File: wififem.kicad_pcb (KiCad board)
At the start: 2 copper layers, 40 x 49.5 mm, 44 parts, among them J1 Conn_Coaxial, J2 Conn_Coaxial, J3 Conn_Coaxial, J4 Conn_01x05, U1 MCP6566, U2 74HCT04, U3 SE2611T, U4 AP1117-15

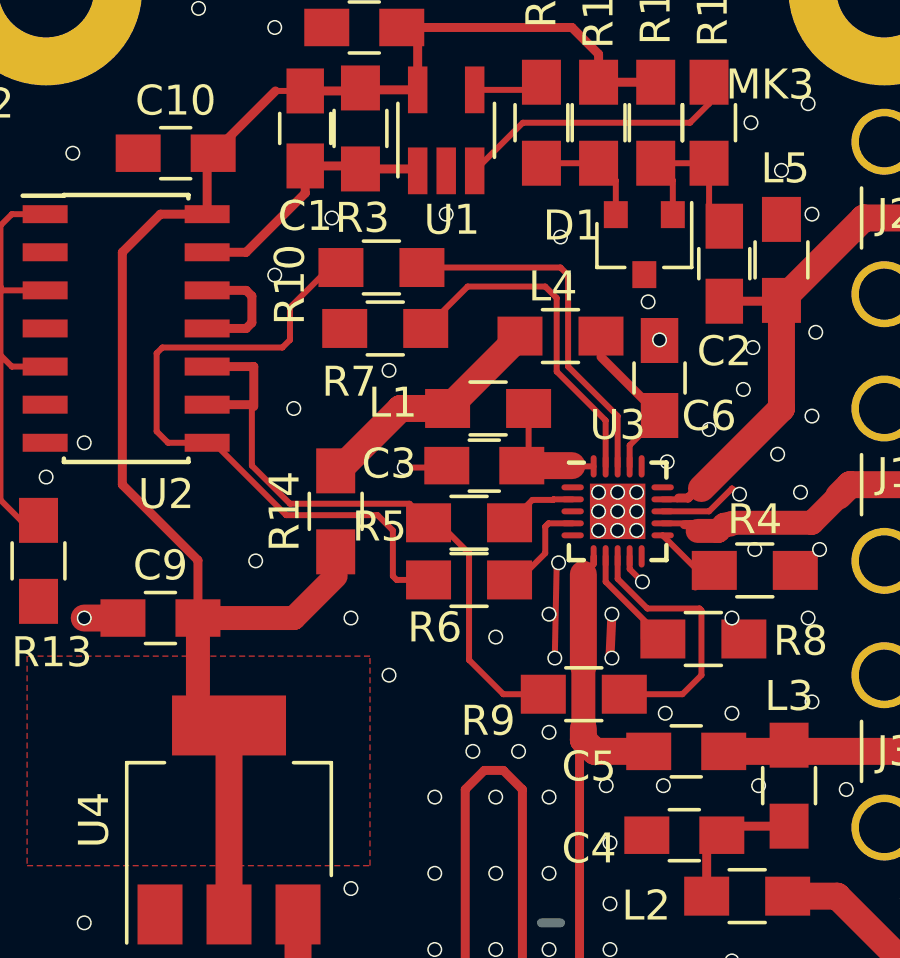
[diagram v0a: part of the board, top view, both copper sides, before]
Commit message: Add LNA on/off jumper
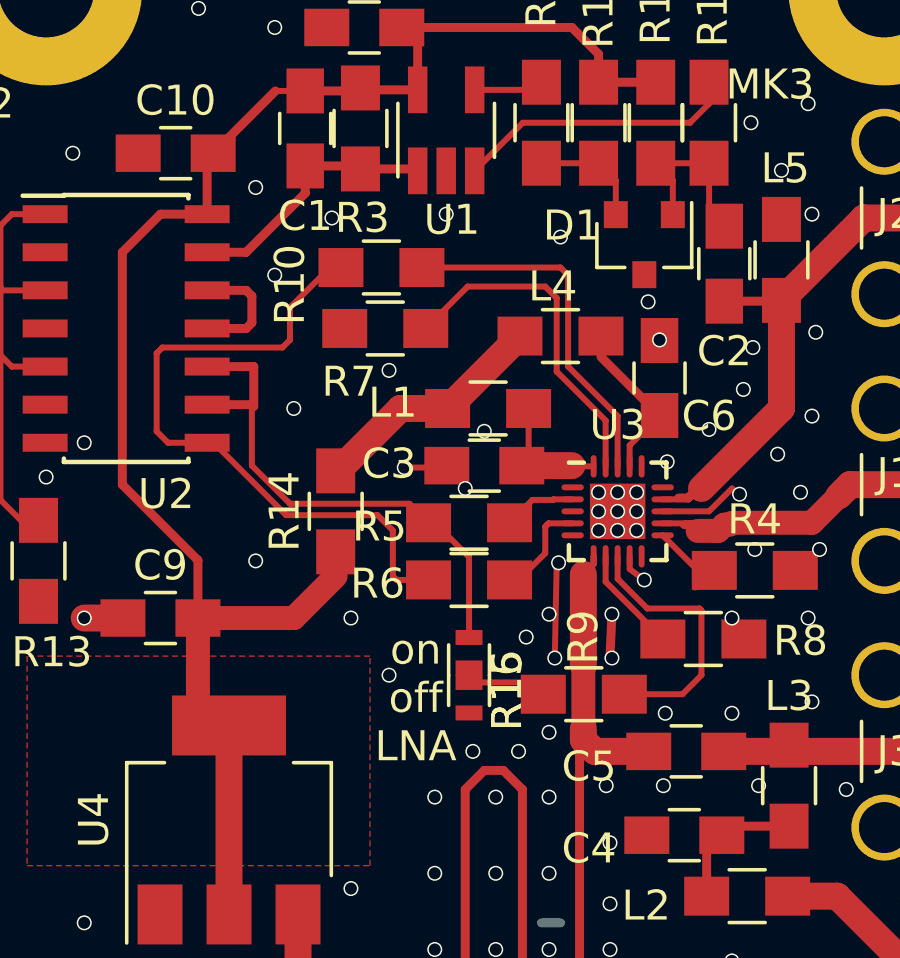
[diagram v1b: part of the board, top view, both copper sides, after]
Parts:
- added R15: 0 (lna off), Resistors_SMD:R_0603, F.Cu at (104.9, 71.4)
- added R16: 0 (lna on), Resistors_SMD:R_0603, F.Cu at (104.9, 70.4)
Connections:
- R5 pad 1: Net-(R5-Pad1) -> Net-(R16-Pad1)
- R9 pad 1: Net-(R5-Pad1) -> Net-(R15-Pad1)
- U2 pad 10: Net-(R5-Pad1) -> Net-(R16-Pad1)
- U2 pad 9: Net-(R5-Pad1) -> Net-(R16-Pad1)
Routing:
- net Net-(R5-Pad1): track 21.5 -> 0.00 mm
- net Net-(R16-Pad1): track 0.00 -> 18.5 mm
- net Net-(R15-Pad1): track 0.00 -> 2.74 mm
- net GND: vias 127 -> 130
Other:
- board text added: "on off LNA"

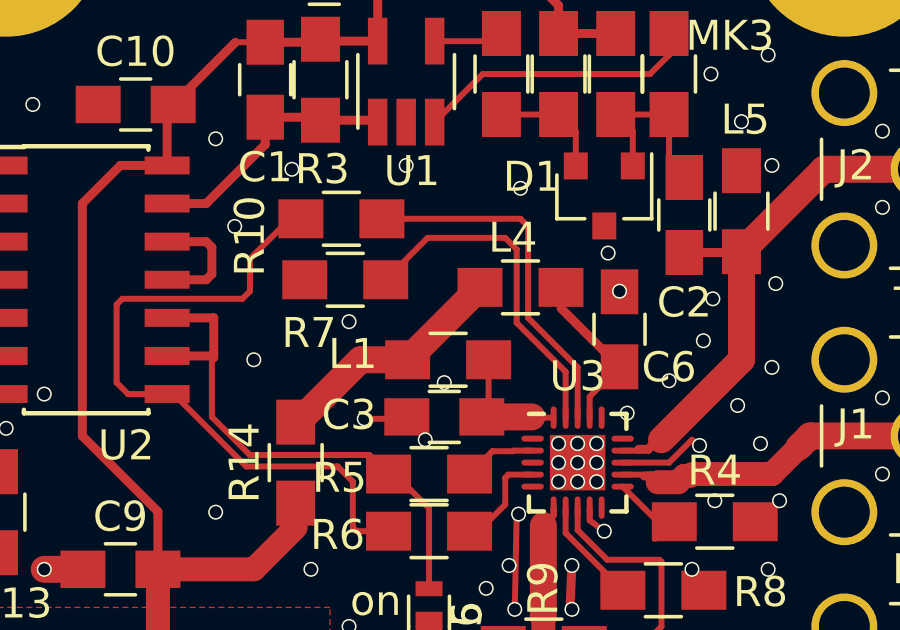
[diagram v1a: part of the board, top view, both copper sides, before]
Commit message: Power supply decoupling as suggested
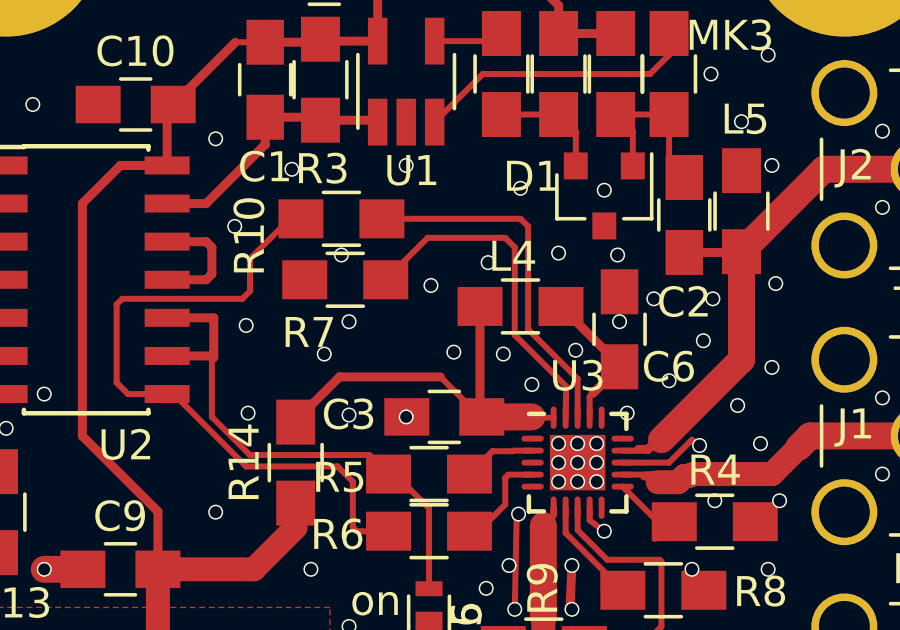
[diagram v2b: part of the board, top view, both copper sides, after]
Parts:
- removed L1: ferrite bead, Inductors_SMD:L_0805_HandSoldering
- moved L4 0.63 mm to (108.0, 60.2)
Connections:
- L4 pad 1: Net-(L1-Pad1) -> Net-(C3-Pad2)
- R14 pad 2: Net-(L1-Pad1) -> Net-(C3-Pad2)
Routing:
- net Net-(C3-Pad2): track 4.40 -> 13.9 mm
- net Net-(L1-Pad1): track 8.00 -> 0.00 mm
- net GND: track 11.4 -> 10.0 mm, vias 130 -> 141
- net Net-(C6-Pad2): track 5.62 -> 4.99 mm

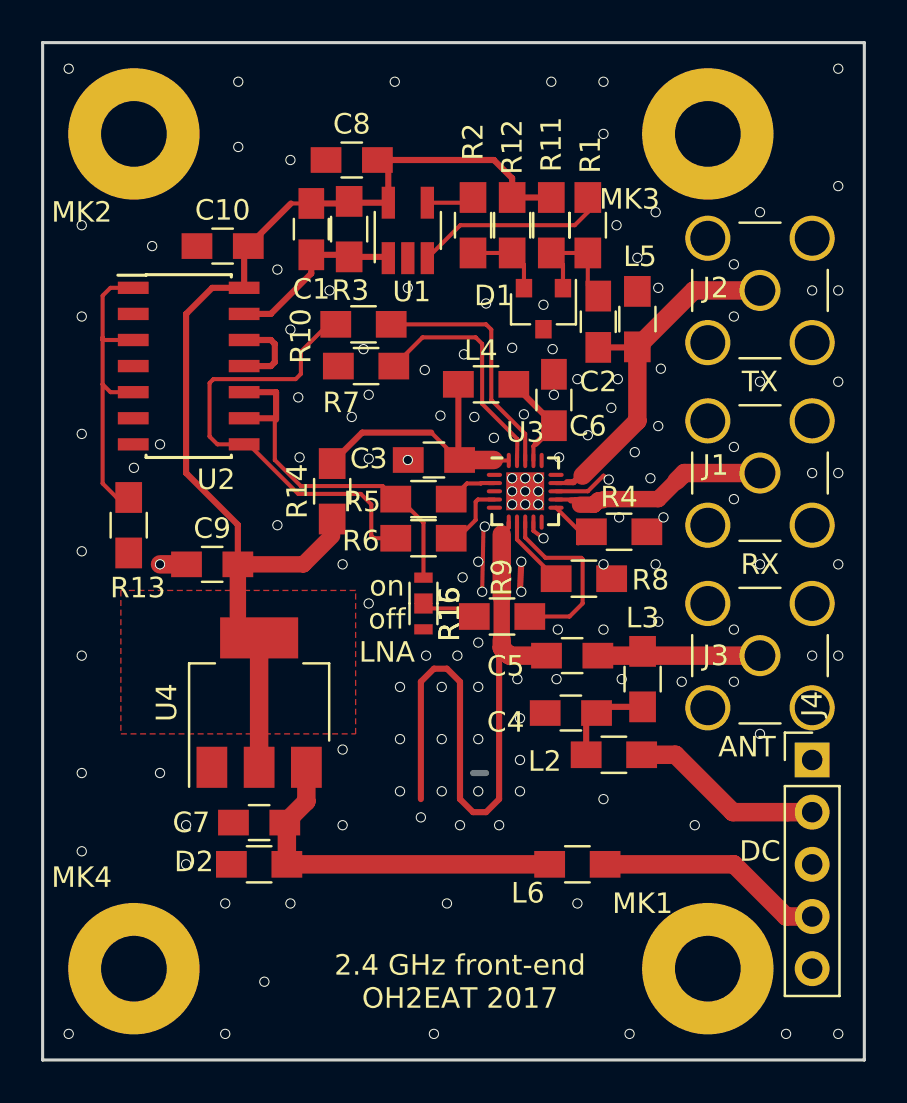
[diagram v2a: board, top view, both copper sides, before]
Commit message: Increased clearance for non-RF traces
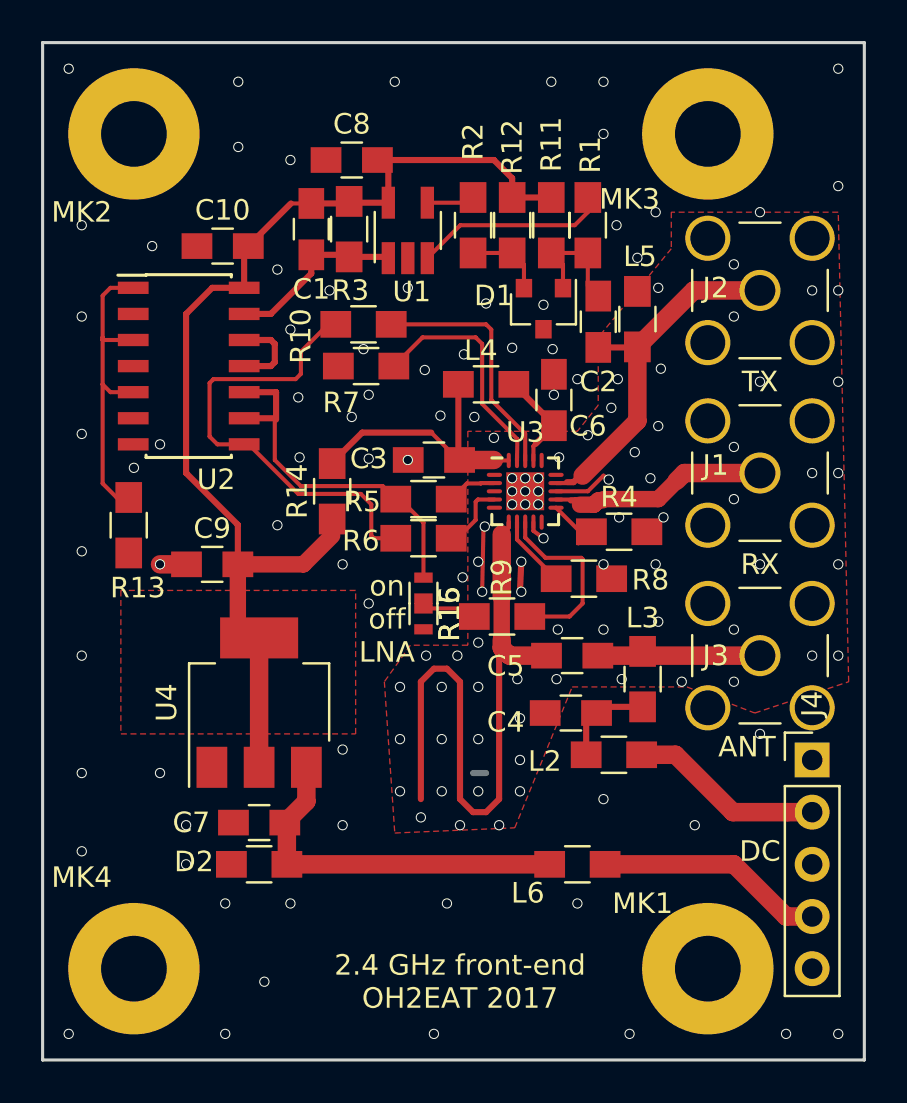
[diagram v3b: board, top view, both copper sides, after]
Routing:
- net GND: vias 141 -> 140
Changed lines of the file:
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@@
     (thickness 1.6)
     (drawings 10)
-    (tracks 372)
+    (tracks 371)
     (zones 0)
     (modules 45)
@@
     (35 F.Paste user hide)
     (36 B.SilkS user hide)
-    (37 F.SilkS user)
+    (37 F.SilkS user hide)
     (38 B.Mask user hide)
     (39 F.Mask user hide)
@@
     (user_trace_width 0.9)
     (trace_clearance 0.1524)
-    (zone_clearance 0)
+    (zone_clearance 0.5)
     (zone_45_only yes)
     (trace_min 0.2)
@@
   (via (at 107.3785 61.7855) (size 0.5) (drill 0.4) (layers F.Cu B.Cu) (net 4))
   (via (at 108.331 62.8015) (size 0.5) (drill 0.4) (layers F.Cu B.Cu) (net 4))
-  (via (at 109.7915 61.6585) (size 0.5) (drill 0.4) (layers F.Cu B.Cu) (net 4))
   (via (at 102.235 63.8175) (size 0.5) (drill 0.4) (layers F.Cu B.Cu) (net 4))
   (via (at 97.79 54.61) (size 0.5) (drill 0.4) (layers F.Cu B.Cu) (net 4))
@@
   (segment (start 107.37724 71.501) (end 107.27724 71.501) (width 0.2) (layer F.Cu) (net 38))
   (zone (net 4) (net_name GND) (layer F.Cu) (hatch edge 0.508)
-    (connect_pads yes (clearance 0.2))
+    (connect_pads yes (clearance 0.5))
     (min_thickness 0.2)
     (fill yes (arc_segments 16) (thermal_gap 0.5) (thermal_bridge_width 0.5))
@@
       )
     )
+  )
+  (zone (net 4) (net_name GND) (layer F.Cu) (hatch edge 0.508)
+    (priority 1)
+    (connect_pads yes (clearance 0.2))
+    (min_thickness 0.2)
+    (fill yes (arc_segments 16) (thermal_gap 0.5) (thermal_bridge_width 0.5))
+    (polygon
+      (pts
+        (xy 125.095 51.816) (xy 116.967 51.816) (xy 116.967 53.594) (xy 113.411 57.912) (xy 113.411 61.214)
+        (xy 112.395 62.484) (xy 107.061 62.484) (xy 107.061 72.898) (xy 104.267 72.898) (xy 102.997 74.676)
+        (xy 103.505 82.042) (xy 109.347 81.788) (xy 112.141 74.93) (xy 117.729 74.93) (xy 121.031 76.2)
+        (xy 125.603 74.676)
+      )
+    )

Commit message: Moved some components a bit
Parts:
- moved L4 0.64 mm to (107.3, 60.2)
- moved C6 0.44 mm to (110.8, 61.0)
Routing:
- net Net-(C6-Pad2): track 4.99 -> 7.08 mm
- net Net-(C5-Pad2): track 33.3 -> 32.7 mm
- net Net-(R10-Pad2): track 12.0 -> 11.5 mm
- net GND: vias 140 -> 141

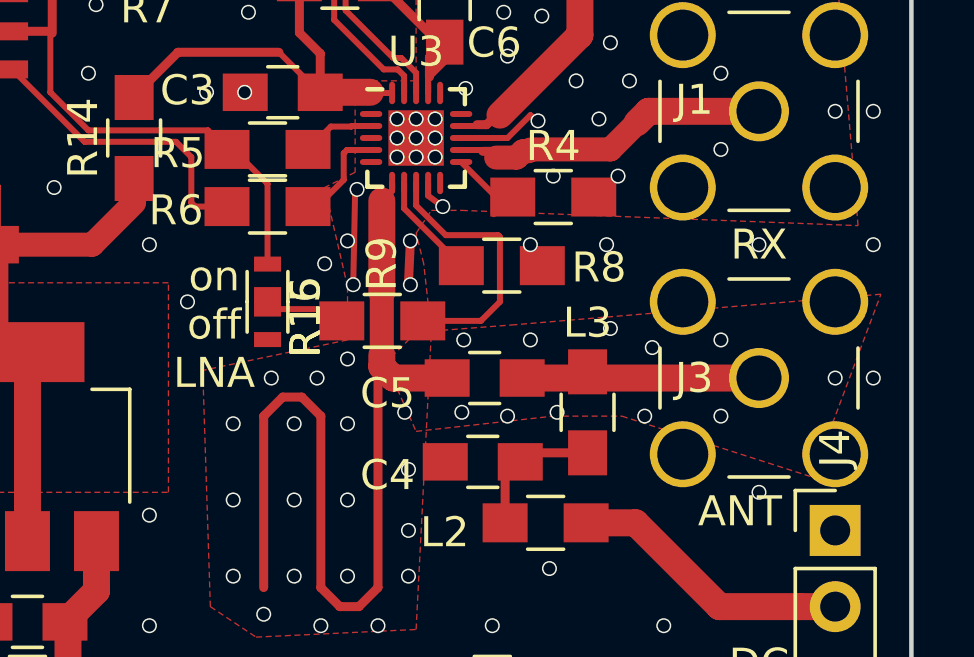
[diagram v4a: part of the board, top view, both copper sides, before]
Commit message: Moved components and copper zone borders again
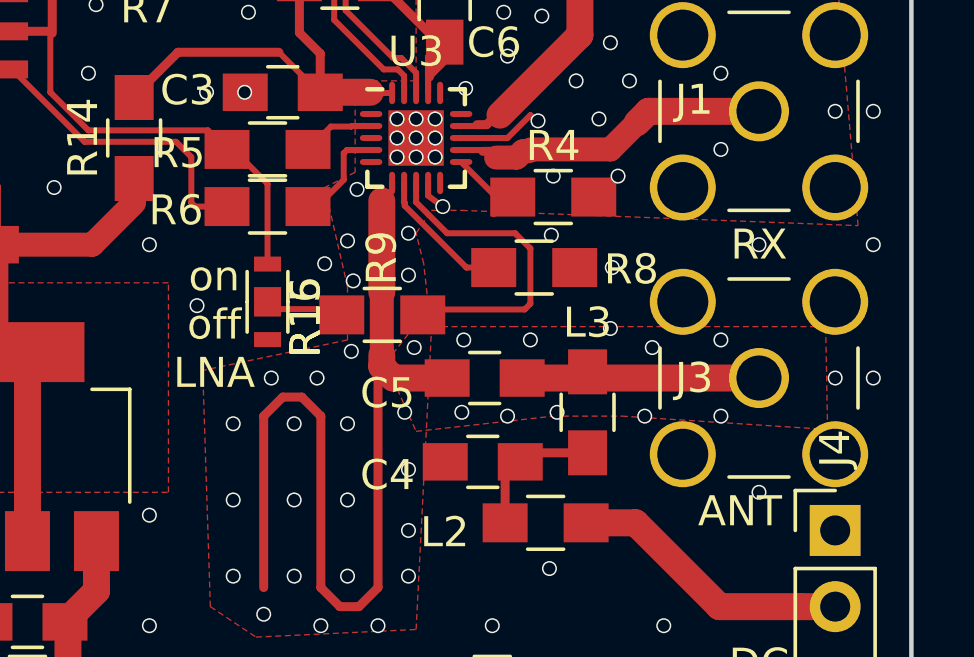
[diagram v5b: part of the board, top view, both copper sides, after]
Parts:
- moved R8 1.08 mm to (113.8, 69.7)
- moved R9 0.20 mm to (108.7, 71.3)
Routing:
- net GND: track 10.0 -> 5.45 mm, vias 141 -> 142
- net Net-(R9-Pad2): track 8.97 -> 10.8 mm

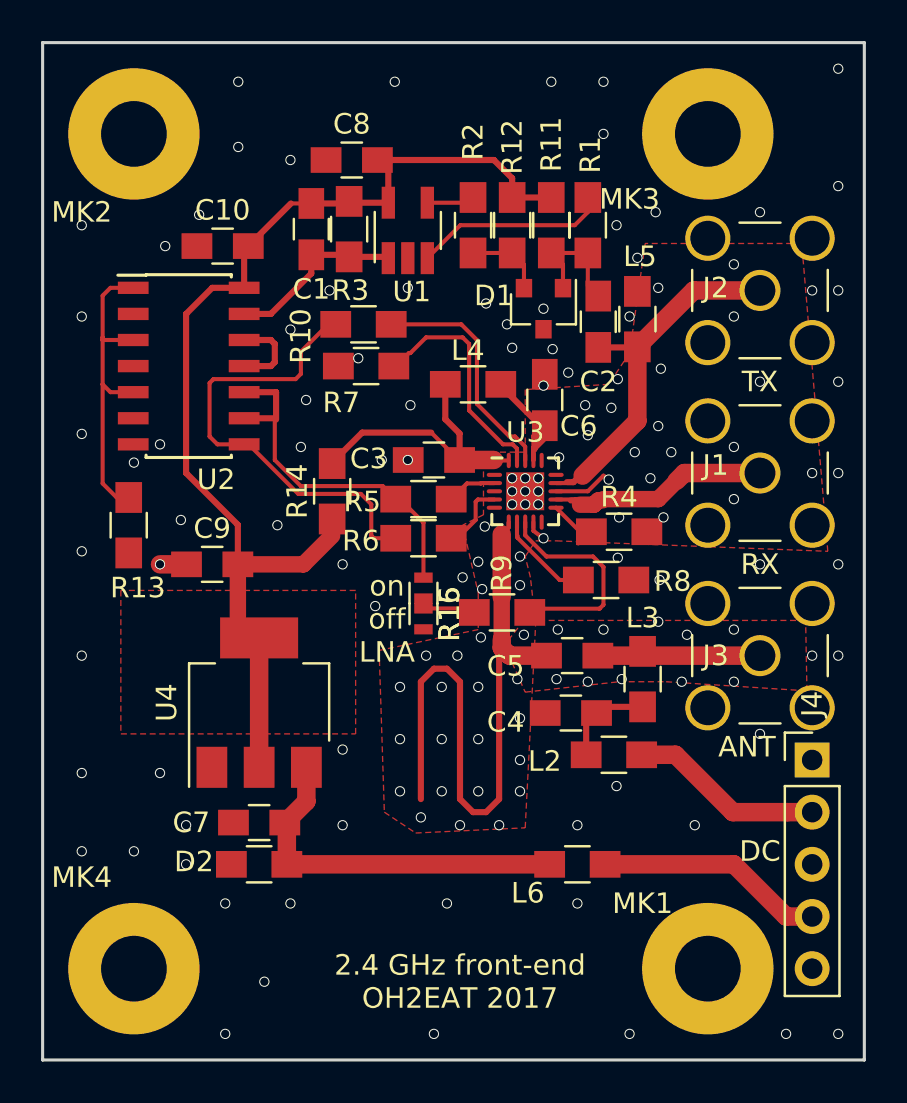
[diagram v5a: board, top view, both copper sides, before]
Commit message: Add DC block capacitors in all RF ports
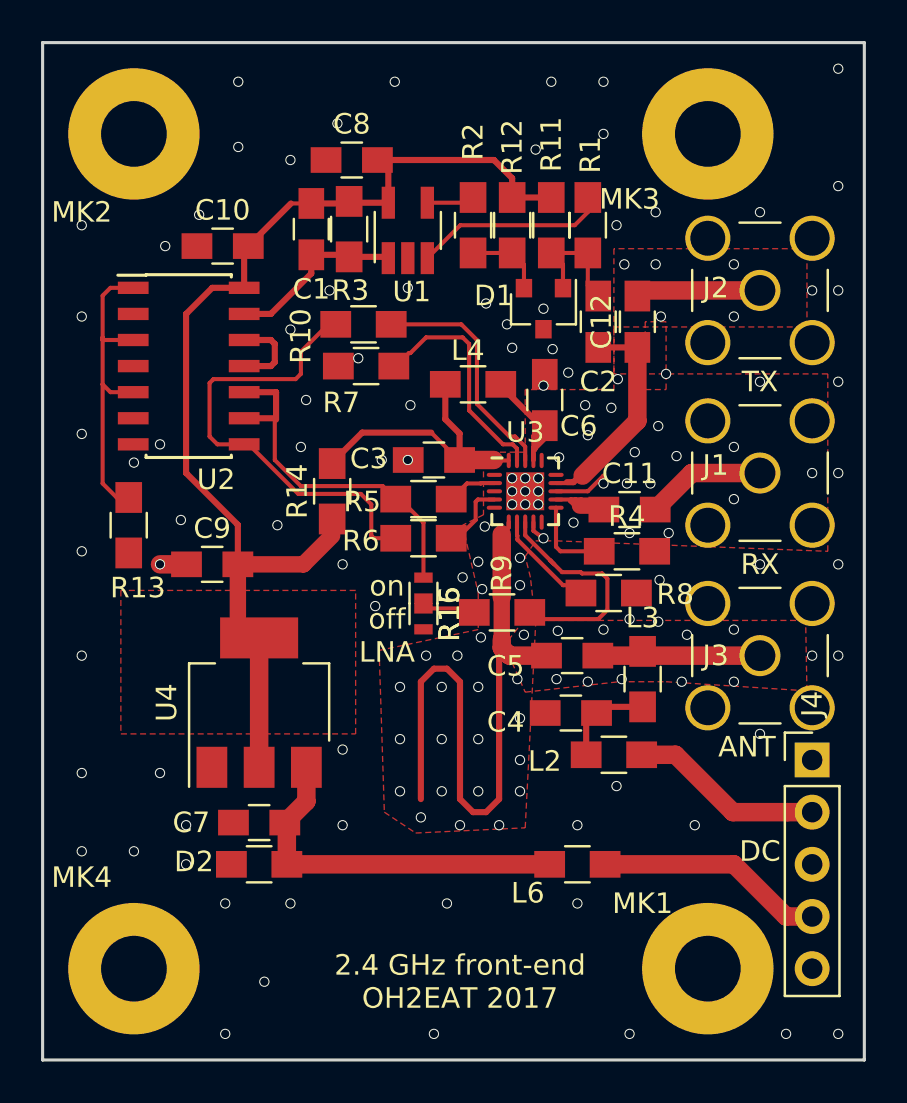
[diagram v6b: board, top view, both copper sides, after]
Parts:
- removed L5: 10n, Inductors_SMD:L_0805_HandSoldering
- added C11: 10p, Capacitors_SMD:C_0805_HandSoldering, F.Cu at (114.9, 66.3)
- added C12: 10p, Capacitors_SMD:C_0805_HandSoldering, F.Cu at (115.3, 57.1)
- moved R4 1.03 mm to (114.8, 68.3)
- moved R8 0.65 mm to (113.9, 70.4)
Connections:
- C2 pad 2: Net-(C2-Pad2) -> Net-(C12-Pad1)
- J1 pad 1: Net-(J1-Pad1) -> Net-(C11-Pad2)
- J2 pad 1: Net-(C2-Pad2) -> Net-(C12-Pad2)
- U3 pad 12: Net-(J1-Pad1) -> Net-(C11-Pad1)
- U3 pad 14: Net-(C2-Pad2) -> Net-(C12-Pad1)
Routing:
- net Net-(C2-Pad2): track 17.8 -> 0.00 mm
- net Net-(J1-Pad1): track 11.0 -> 0.00 mm
- net Net-(C12-Pad1): track 0.00 -> 10.7 mm
- net Net-(C12-Pad2): track 0.00 -> 6.08 mm
- net Net-(C11-Pad2): track 0.00 -> 5.84 mm
- net Net-(C11-Pad1): track 0.00 -> 3.70 mm
- net Net-(R4-Pad1): track 2.86 -> 4.10 mm
- net Net-(R9-Pad2): track 10.8 -> 11.4 mm
- net GND: track 5.45 -> 5.51 mm, vias 142 -> 146
